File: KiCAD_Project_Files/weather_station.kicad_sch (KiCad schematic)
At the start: 57 parts, among them J1 JST-XH, J2 SMA Antenna Connector, J3 Debug Connector, SW1 SW_MAIN_PWR, U1 RFM95W-868S2R, U10 TPS61023DRLR, U2 MICS-6814, U3 STM32F301C8T6TR, U4 KP254, U5 HIH6020-021-001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

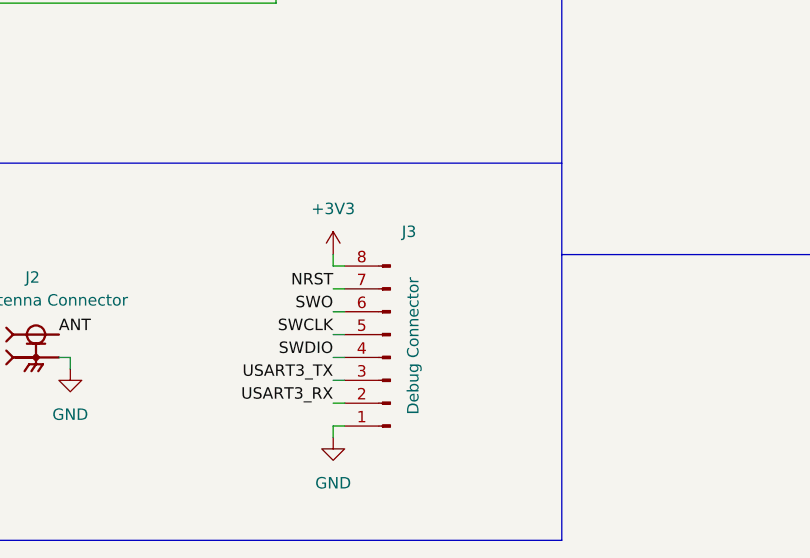
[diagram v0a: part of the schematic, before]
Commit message: Updated PCB and added 3D view
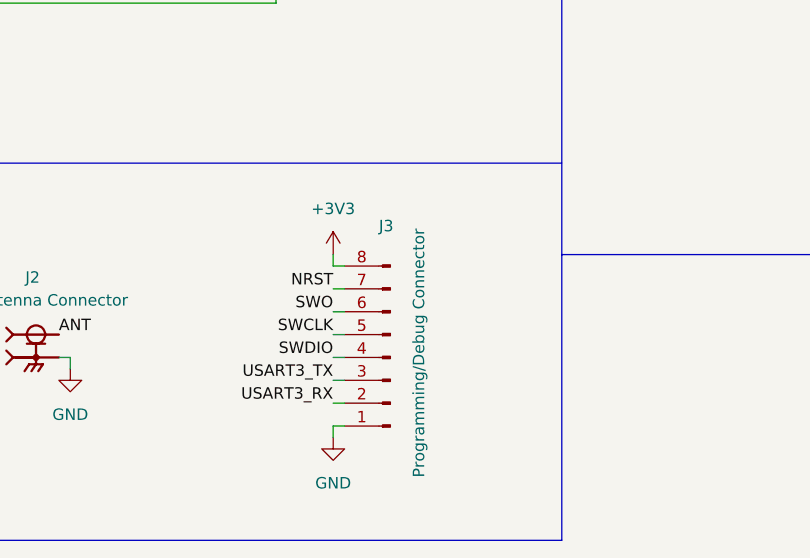
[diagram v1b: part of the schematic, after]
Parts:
- J3: value Debug Connector -> Programming/Debug Connector
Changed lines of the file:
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@@
     (rev "0.1")
     (company "Politechnika Poznańska")
-    (comment 1 "Jakub Grzesiak")
-    (comment 2 "Author:")
+    (comment 1 "Jakub Grzesiak, 144516")
+    (comment 3 "Author:")
   )
   (junction (at 132.08 73.66) (diameter 0) (color 0 0 0 0)
@@
   (symbol (lib_id "Connector:Conn_01x08_Male") (at 276.86 260.35 180) (unit 1)
     (in_bom yes) (on_board yes)
-    (property "Reference" "J3" (id 0) (at 278.13 246.38 0)
+    (property "Reference" "J3" (id 0) (at 275.59 245.745 0)
       (effects (font (size 1.27 1.27)) (justify right))
     )
-    (property "Value" "Debug Connector" (id 1) (at 279.4 266.7 90)
+    (property "Value" "Programming/Debug Connector" (id 1) (at 280.035 273.685 90)
       (effects (font (size 1.27 1.27)) (justify right))
     )
@@
       (effects (font (size 1.27 1.27)) (justify left bottom) hide)
     )
-    (property "Datasheet" "" (id 3) (at 52.07 135.89 0)
+    (property "Datasheet" "https://abracon.com/Resonators/ABM3.pdf" (id 3) (at 52.07 135.89 0)
       (effects (font (size 1.27 1.27)) (justify left bottom) hide)
     )
@@
     )
     (path "/62da85fe-7151-4267-850f-1a9c091e652b"
-      (reference "J3") (unit 1) (value "Debug Connector") (footprint "Connector_PinHeader_1.27mm:PinHeader_1x08_P1.27mm_Vertical")
+      (reference "J3") (unit 1) (value "Programming/Debug Connector") (footprint "Connector_PinHeader_1.27mm:PinHeader_1x08_P1.27mm_Vertical")
     )
     (path "/fe7823e8-27a0-4c50-9e85-231b4c296c96"
